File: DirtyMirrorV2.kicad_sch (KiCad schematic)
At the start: 72 parts, among them J1 PWR, J2 ScopeGroundLoop, SW1 SW_SPDT, U1 TL072, U2 TL074, U3 TL074

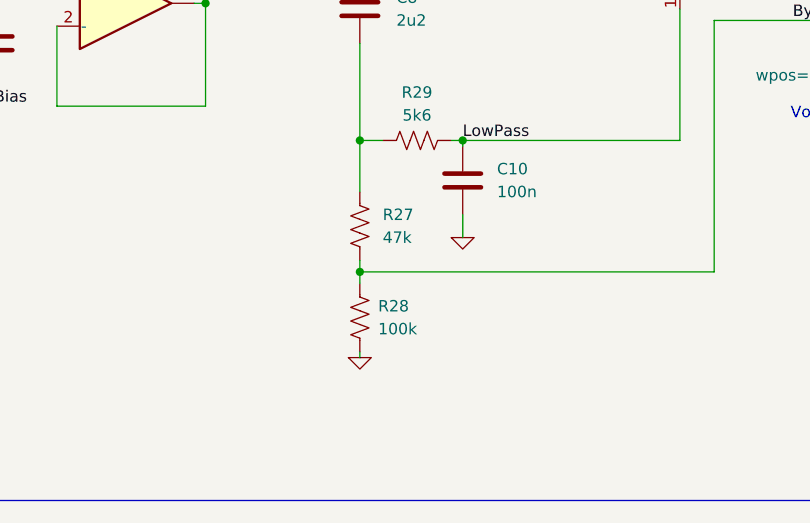
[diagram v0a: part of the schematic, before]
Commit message: switched tone bypass voltage divider
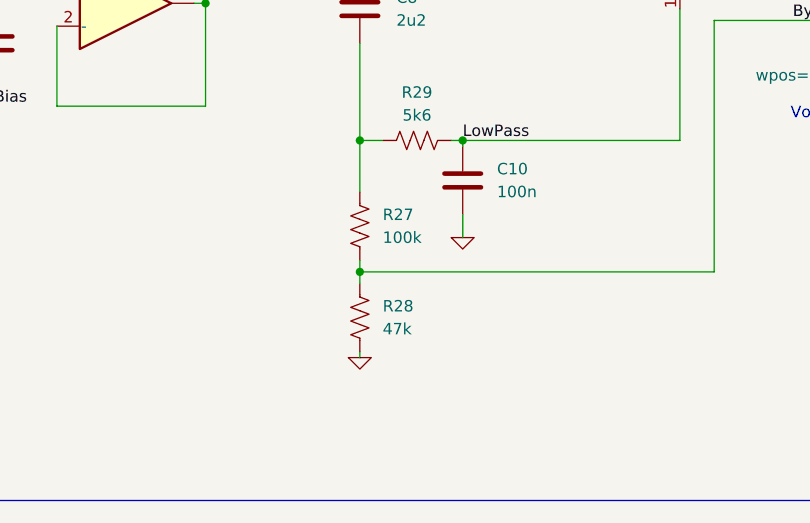
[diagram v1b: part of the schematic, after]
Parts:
- R27: value 47k -> 100k
- R28: value 100k -> 47k
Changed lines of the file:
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@@
 		(fields_autoplaced yes)
 		(property "Reference" "R28"
-			(at 299.212 200.6599 0)
+			(at 299.72 200.6599 0)
 			(show_name no)
 			(do_not_autoplace no)
@@
 			)
 		)
-		(property "Value" "100k"
-			(at 299.212 203.1999 0)
+		(property "Value" "47k"
+			(at 299.72 203.1999 0)
 			(show_name no)
 			(do_not_autoplace no)
@@
 			)
 		)
-		(property "Value" "47k"
+		(property "Value" "100k"
 			(at 299.72 193.0399 0)
 			(show_name no)

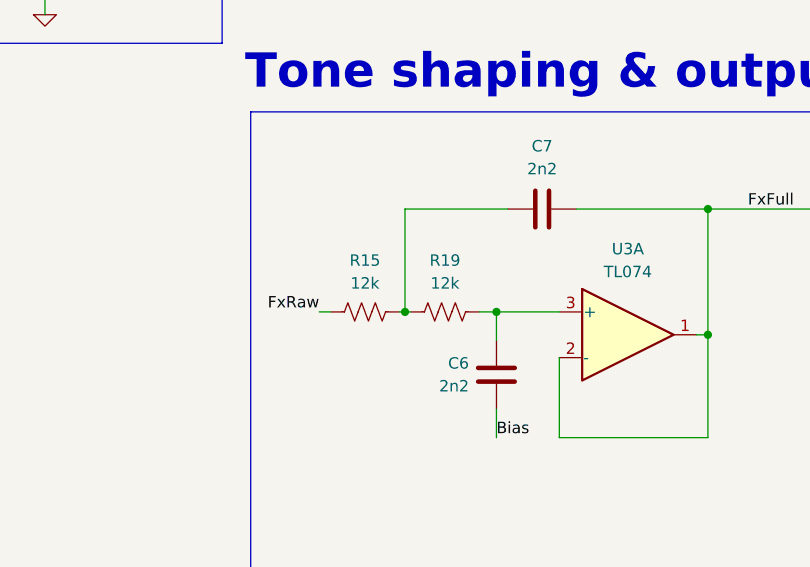
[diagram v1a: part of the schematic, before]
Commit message: de-hissing butterworth changes
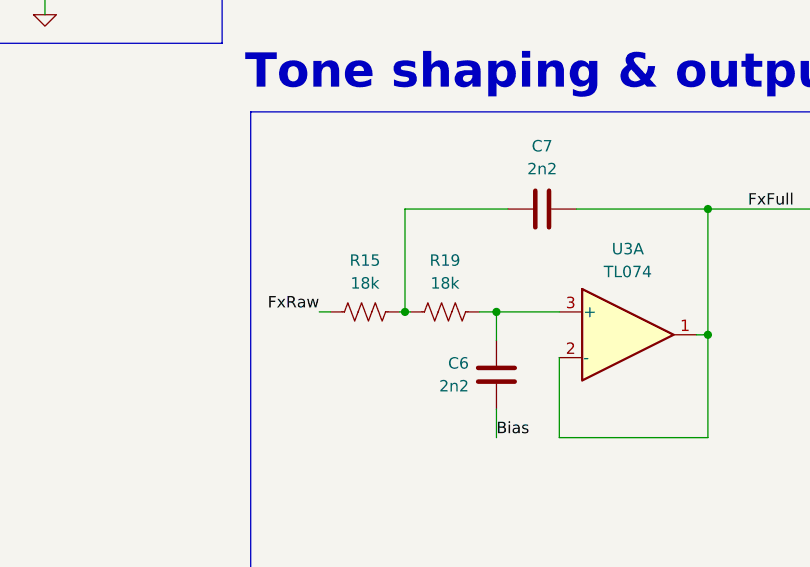
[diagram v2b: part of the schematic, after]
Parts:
- R15, R19: value 12k -> 18k
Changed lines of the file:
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@@
 			)
 		)
-		(property "Value" "12k"
+		(property "Value" "18k"
 			(at 241.935 161.29 90)
 			(show_name no)
@@
 			)
 		)
-		(property "Value" "12k"
+		(property "Value" "18k"
 			(at 250.825 161.29 90)
 			(show_name no)
